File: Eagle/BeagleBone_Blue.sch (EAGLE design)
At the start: 293 parts, among them M1 JST_ZH_2, M2 JST_ZH_2, M3 JST_ZH_2, M4 JST_ZH_2, Q3 MOSFET-N, U1 TPD4S012_DRY_6, U2 CM200C-32.768KAZF-UT, U3 SCHA5B0200, U4 TPD4S012_DRY_6, U5 24LC_32AT-I/OT, U6 SN74LVC1G07_DCK_5, U7 TPS2051B_D_8, Y2 445C33D24M00000

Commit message: Update title block
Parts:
- U6: device SN74LVC1G07:SN74LVC1G07_DCK_5 -> BeagleBone_Blue:SN74LVC1G07_DCK_5
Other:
- note added: "This schematic is *NOT SUPPORTED* and DOES NOT constitute a reference design. Only *community* support is allowed via resources at BeagleBoard.org/discuss. THERE IS NO WARRANTY FOR THIS DESIGN, TO THE EXTENT PERMITTED BY APPLICABLE LAW. EXCEPT WHEN OTHERWISE STATED IN WRITING THE COPYRIGHT HOLDERS AND/OR OTHER PARTIES PROVIDE THE DESIGN *AS IS* WITHOUT WARRANTY OF ANY KIND, EITHER EXPRESSED OR IM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"

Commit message: Update license
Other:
- note added: "This work is licensed under a Creative Commons Attribution-ShareAlike 3.0 United States License."
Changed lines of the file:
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@@
 THE DESIGN PROVE DEFECTIVE, YOU ASSUME THE COST
 OF ALL NECESSARY SERVICING, REPAIR OR CORRECTION. </text>
+<text x="5.08" y="182.88" size="1.778" layer="91">This work is licensed under a Creative Commons
+Attribution-ShareAlike 3.0 United States License.
+</text>
 </plain>
 <instances>

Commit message: Add GNDs
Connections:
- new net N$131: SIPF.DGND1, SIPF.DGND10, SIPF.DGND11, SIPF.DGND12, SIPF.DGND13, SIPF.DGND14, SIPF.DGND15, SIPF.DGND16, SIPF.DGND17, SIPF.DGND18, SIPF.DGND19, SIPF.DGND2, SIPF.DGND20, SIPF.DGND21, SIPF.DGND22, SIPF.DGND23, SIPF.DGND24, SIPF.DGND25, SIPF.DGND26, SIPF.DGND27, SIPF.DGND28, SIPF.DGND29, SIPF.DGND3, SIPF.DGND30, SIPF.DGND31, SIPF.DGND32, SIPF.DGND33, SIPF.DGND34, SIPF.DGND35, SIPF.DGND36, SIPF.DGND38, SIPF.DGND39, SIPF.DGND4, SIPF.DGND40, SIPF.DGND41, SIPF.DGND42, SIPF.DGND43, SIPF.DGND44, SIPF.DGND45, SIPF.DGND46, SIPF.DGND47, SIPF.DGND48, SIPF.DGND49, SIPF.DGND5, SIPF.DGND50, SIPF.DGND51, SIPF.DGND52, SIPF.DGND53, SIPF.DGND54, SIPF.DGND55, SIPF.DGND56, SIPF.DGND57, SIPF.DGND58, SIPF.DGND59, SIPF.DGND6, SIPF.DGND60, SIPF.DGND61, SIPF.DGND62, SIPF.DGND63, SIPF.DGND65, SIPF.DGND66, SIPF.DGND67, SIPF.DGND68, SIPF.DGND69, SIPF.DGND7, SIPF.DGND70, SIPF.DGND71, SIPF.DGND72, SIPF.DGND73, SIPF.DGND74, SIPF.DGND75, SIPF.DGND76, SIPF.DGND77, SIPF.DGND78, SIPF.DGND79, SIPF.DGND8, SIPF.DGND80, SIPF.DGND82, SIPF.DGND83, SIPF.DGND84, SIPF.DGND85, SIPF.DGND86, SIPF.DGND9

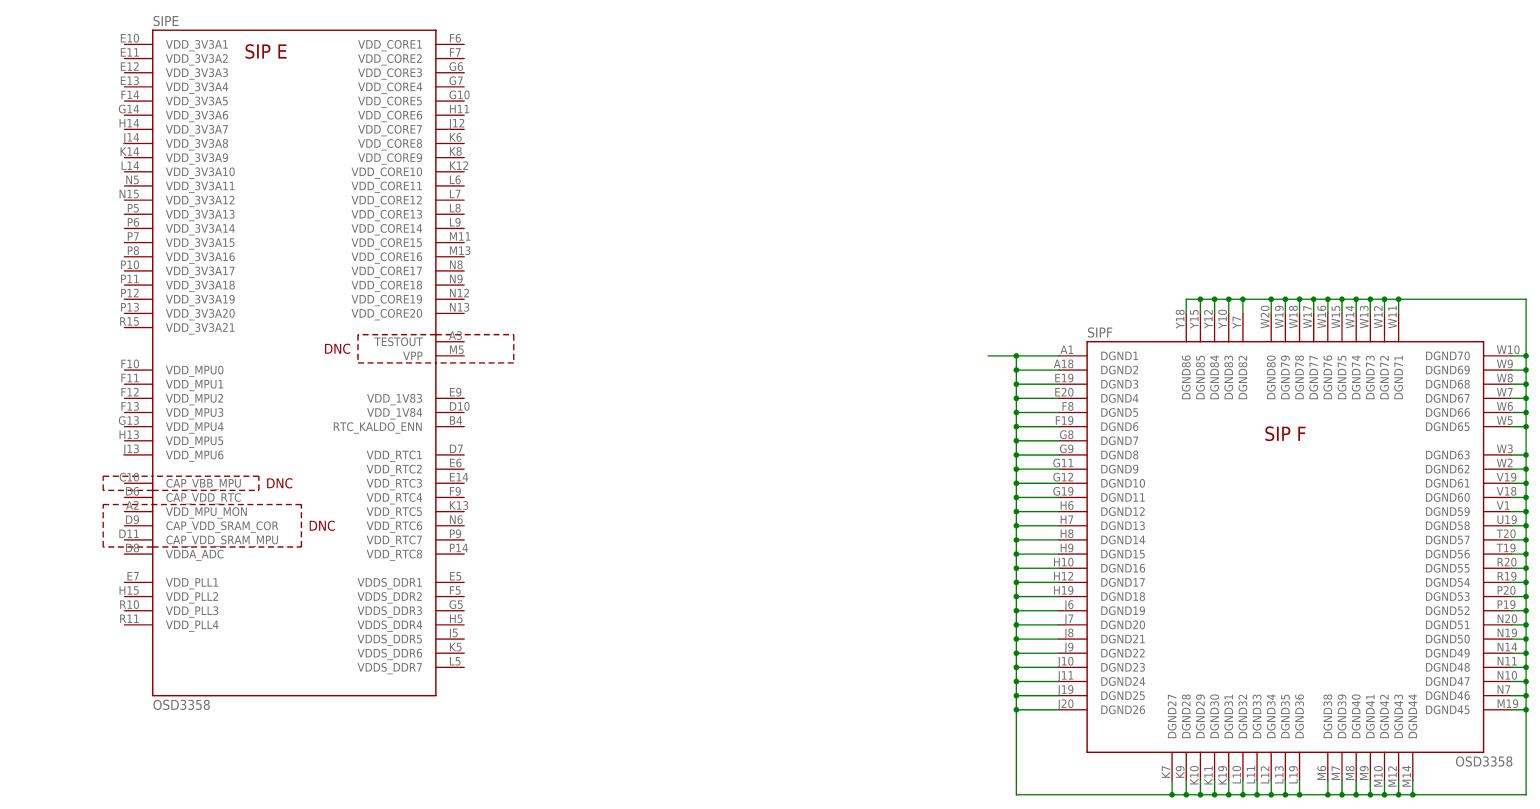
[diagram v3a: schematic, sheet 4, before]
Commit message: Complete power connections
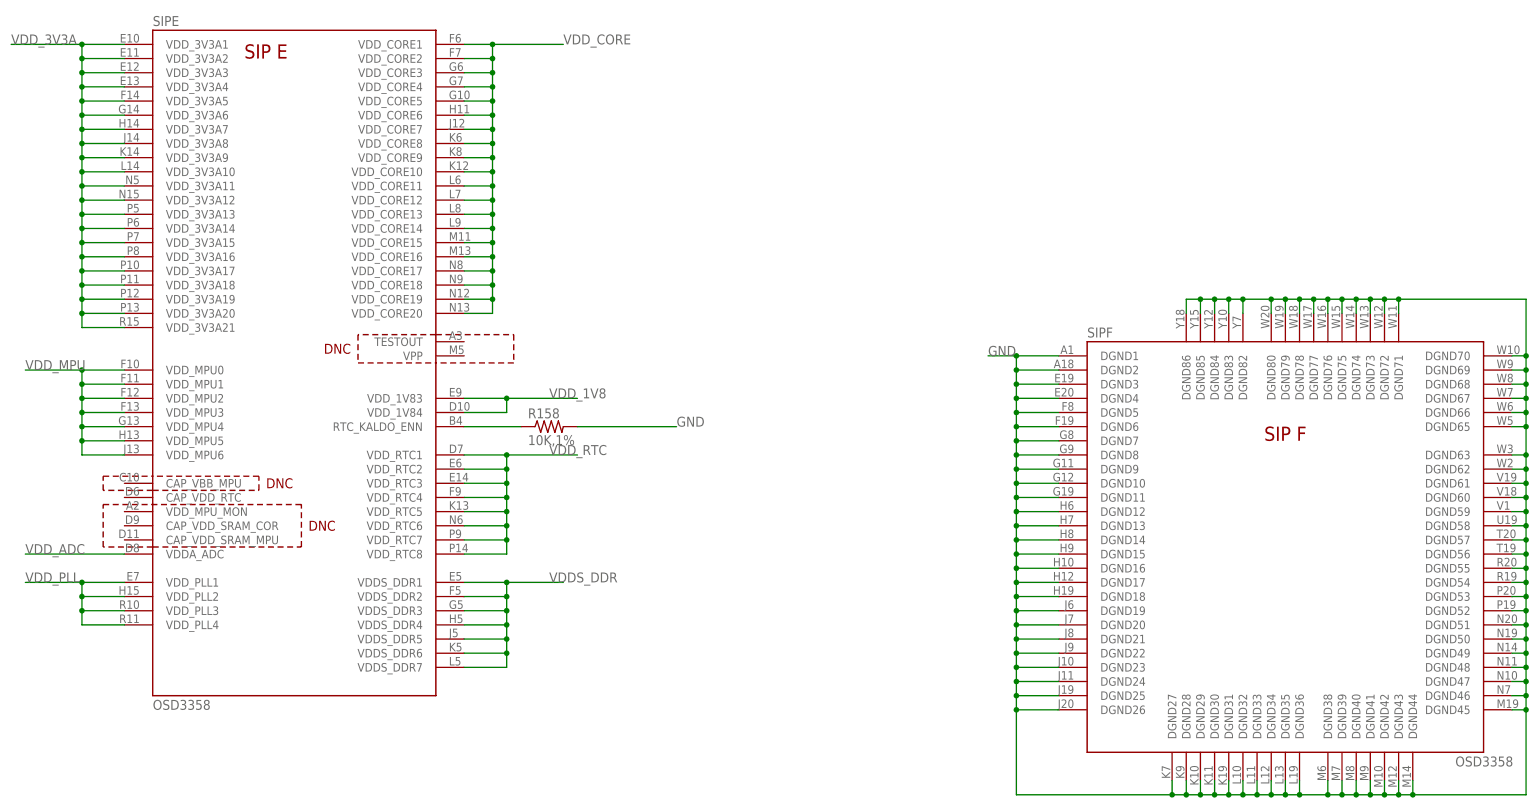
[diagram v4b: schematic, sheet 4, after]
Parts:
- added R158: 10K,1%, Strawson_Eagle_Lib:RESISTOR0402-RES
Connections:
- new net VDDS_DDR: SIPE.VDDS_DDR1, SIPE.VDDS_DDR2, SIPE.VDDS_DDR3, SIPE.VDDS_DDR4, SIPE.VDDS_DDR5, SIPE.VDDS_DDR6, SIPE.VDDS_DDR7
- new net VDD_CORE: SIPE.VDD_CORE1, SIPE.VDD_CORE10, SIPE.VDD_CORE11, SIPE.VDD_CORE12, SIPE.VDD_CORE13, SIPE.VDD_CORE14, SIPE.VDD_CORE15, SIPE.VDD_CORE16, SIPE.VDD_CORE17, SIPE.VDD_CORE18, SIPE.VDD_CORE19, SIPE.VDD_CORE2, SIPE.VDD_CORE20, SIPE.VDD_CORE3, SIPE.VDD_CORE4, SIPE.VDD_CORE5, SIPE.VDD_CORE6, SIPE.VDD_CORE7, SIPE.VDD_CORE8, SIPE.VDD_CORE9
- new net VDD_MPU: SIPE.VDD_MPU0, SIPE.VDD_MPU1, SIPE.VDD_MPU2, SIPE.VDD_MPU3, SIPE.VDD_MPU4, SIPE.VDD_MPU5, SIPE.VDD_MPU6
- new net VDD_PLL: SIPE.VDD_PLL1, SIPE.VDD_PLL2, SIPE.VDD_PLL3, SIPE.VDD_PLL4
- net GND: now also R158.2, SIPF.DGND1, SIPF.DGND10, SIPF.DGND11, SIPF.DGND12, SIPF.DGND13, SIPF.DGND14, SIPF.DGND15, SIPF.DGND16, SIPF.DGND17, SIPF.DGND18, SIPF.DGND19, SIPF.DGND2, SIPF.DGND20, SIPF.DGND21, SIPF.DGND22, SIPF.DGND23, SIPF.DGND24, SIPF.DGND25, SIPF.DGND26, SIPF.DGND27, SIPF.DGND28, SIPF.DGND29, SIPF.DGND3, SIPF.DGND30, SIPF.DGND31, SIPF.DGND32, SIPF.DGND33, SIPF.DGND34, SIPF.DGND35, SIPF.DGND36, SIPF.DGND38, SIPF.DGND39, SIPF.DGND4, SIPF.DGND40, SIPF.DGND41, SIPF.DGND42, SIPF.DGND43, SIPF.DGND44, SIPF.DGND45, SIPF.DGND46, SIPF.DGND47, SIPF.DGND48, SIPF.DGND49, SIPF.DGND5, SIPF.DGND50, SIPF.DGND51, SIPF.DGND52, SIPF.DGND53, SIPF.DGND54, SIPF.DGND55, SIPF.DGND56, SIPF.DGND57, SIPF.DGND58, SIPF.DGND59, SIPF.DGND6, SIPF.DGND60, SIPF.DGND61, SIPF.DGND62, SIPF.DGND63, SIPF.DGND65, SIPF.DGND66, SIPF.DGND67, SIPF.DGND68, SIPF.DGND69, SIPF.DGND7, SIPF.DGND70, SIPF.DGND71, SIPF.DGND72, SIPF.DGND73, SIPF.DGND74, SIPF.DGND75, SIPF.DGND76, SIPF.DGND77, SIPF.DGND78, SIPF.DGND79, SIPF.DGND8, SIPF.DGND80, SIPF.DGND82, SIPF.DGND83, SIPF.DGND84, SIPF.DGND85, SIPF.DGND86, SIPF.DGND9
- net N$131: now also R158.1, SIPE.RTC_KALDO_ENN; no longer SIPF.DGND1, SIPF.DGND10, SIPF.DGND11, SIPF.DGND12, SIPF.DGND13, SIPF.DGND14, SIPF.DGND15, SIPF.DGND16, SIPF.DGND17, SIPF.DGND18, SIPF.DGND19, SIPF.DGND2, SIPF.DGND20, SIPF.DGND21, SIPF.DGND22, SIPF.DGND23, SIPF.DGND24, SIPF.DGND25, SIPF.DGND26, SIPF.DGND27, SIPF.DGND28, SIPF.DGND29, SIPF.DGND3, SIPF.DGND30, SIPF.DGND31, SIPF.DGND32, SIPF.DGND33, SIPF.DGND34, SIPF.DGND35, SIPF.DGND36, SIPF.DGND38, SIPF.DGND39, SIPF.DGND4, SIPF.DGND40, SIPF.DGND41, SIPF.DGND42, SIPF.DGND43, SIPF.DGND44, SIPF.DGND45, SIPF.DGND46, SIPF.DGND47, SIPF.DGND48, SIPF.DGND49, SIPF.DGND5, SIPF.DGND50, SIPF.DGND51, SIPF.DGND52, SIPF.DGND53, SIPF.DGND54, SIPF.DGND55, SIPF.DGND56, SIPF.DGND57, SIPF.DGND58, SIPF.DGND59, SIPF.DGND6, SIPF.DGND60, SIPF.DGND61, SIPF.DGND62, SIPF.DGND63, SIPF.DGND65, SIPF.DGND66, SIPF.DGND67, SIPF.DGND68, SIPF.DGND69, SIPF.DGND7, SIPF.DGND70, SIPF.DGND71, SIPF.DGND72, SIPF.DGND73, SIPF.DGND74, SIPF.DGND75, SIPF.DGND76, SIPF.DGND77, SIPF.DGND78, SIPF.DGND79, SIPF.DGND8, SIPF.DGND80, SIPF.DGND82, SIPF.DGND83, SIPF.DGND84, SIPF.DGND85, SIPF.DGND86, SIPF.DGND9
- net VDD_1V8: now also SIPE.VDD_1V83, SIPE.VDD_1V84
- net VDD_3V3A: now also SIPE.VDD_3V3A1, SIPE.VDD_3V3A10, SIPE.VDD_3V3A11, SIPE.VDD_3V3A12, SIPE.VDD_3V3A13, SIPE.VDD_3V3A14, SIPE.VDD_3V3A15, SIPE.VDD_3V3A16, SIPE.VDD_3V3A17, SIPE.VDD_3V3A18, SIPE.VDD_3V3A19, SIPE.VDD_3V3A2, SIPE.VDD_3V3A20, SIPE.VDD_3V3A21, SIPE.VDD_3V3A3, SIPE.VDD_3V3A4, SIPE.VDD_3V3A5, SIPE.VDD_3V3A6, SIPE.VDD_3V3A7, SIPE.VDD_3V3A8, SIPE.VDD_3V3A9
- net VDD_ADC: now also SIPE.VDDA_ADC
- net VDD_RTC: now also SIPE.VDD_RTC1, SIPE.VDD_RTC2, SIPE.VDD_RTC3, SIPE.VDD_RTC4, SIPE.VDD_RTC5, SIPE.VDD_RTC6, SIPE.VDD_RTC7, SIPE.VDD_RTC8

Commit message: Fixing some ERCs
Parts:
- renumbered U$3 to U8, U2 to Y1, U3 to P10
